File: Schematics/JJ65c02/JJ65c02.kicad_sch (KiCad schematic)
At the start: 21 parts, among them SW1 RESET, U1 74HC00

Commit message: More work on rp2040-version2
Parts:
- removed RN1: 4.7K, Resistor_THT:R_Array_SIP6, symbol Device:R_Network06_Split
- added R10, R18, R19, R8, R9: 4.7K, Resistor_THT:R_Axial_DIN0207_L6.3mm_D2.5mm_P7.62mm_Horizontal, symbol Device:R
- RAM1: footprint JJ65c02:DIP1524W45P254L4191H419Q32 -> DIP1524W45P254L4191H419Q32
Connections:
- net +5V: now also R10.1, R18.1, R19.2, R8.2, R9.2
- net GND: now also ROM1.2 (A16)
- net a15: now also ROM1.3 (A15)
- net at CPU1.2 (RDY): now also R8.1
- net at CPU1.36 (BE): now also R10.2
- net at CPU1.6 (~{NMI}): now also R9.1
- net at RAM1.30 (CE2): now also R18.2
- net at ROM1.31 (PGM): now also R19.1
- no-connect marks 24 -> 22

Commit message: Latest Kicad schematics and PCB
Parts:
- removed R10, R18, R19, R8, R9: 4.7K, Resistor_THT:R_Axial_DIN0207_L6.3mm_D2.5mm_P7.62mm_Horizontal, symbol Device:R
- added RN1, RN2: 4.7k, Resistor_THT:R_Array_SIP6, symbol Device:R_Pack03_SIP_Split
- RAM1: footprint DIP1524W45P254L4191H419Q32 -> Package_DIP:DIP-32_W15.24mm_Socket
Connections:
- net +5V: now also RN1.1 (R1.1), RN1.3 (R2.1), RN1.5 (R3.1), RN2.1 (R1.1), RN2.3 (R2.1)
- net at CPU1.2 (RDY): now also RN1.2 (R1.2)
- net at CPU1.36 (BE): now also RN1.4 (R2.2)
- net at CPU1.6 (~{NMI}): now also RN1.6 (R3.2)
- net at RAM1.30 (CE2): now also RN2.2 (R1.2)
- net at ROM1.31 (PGM): now also RN2.4 (R2.2)

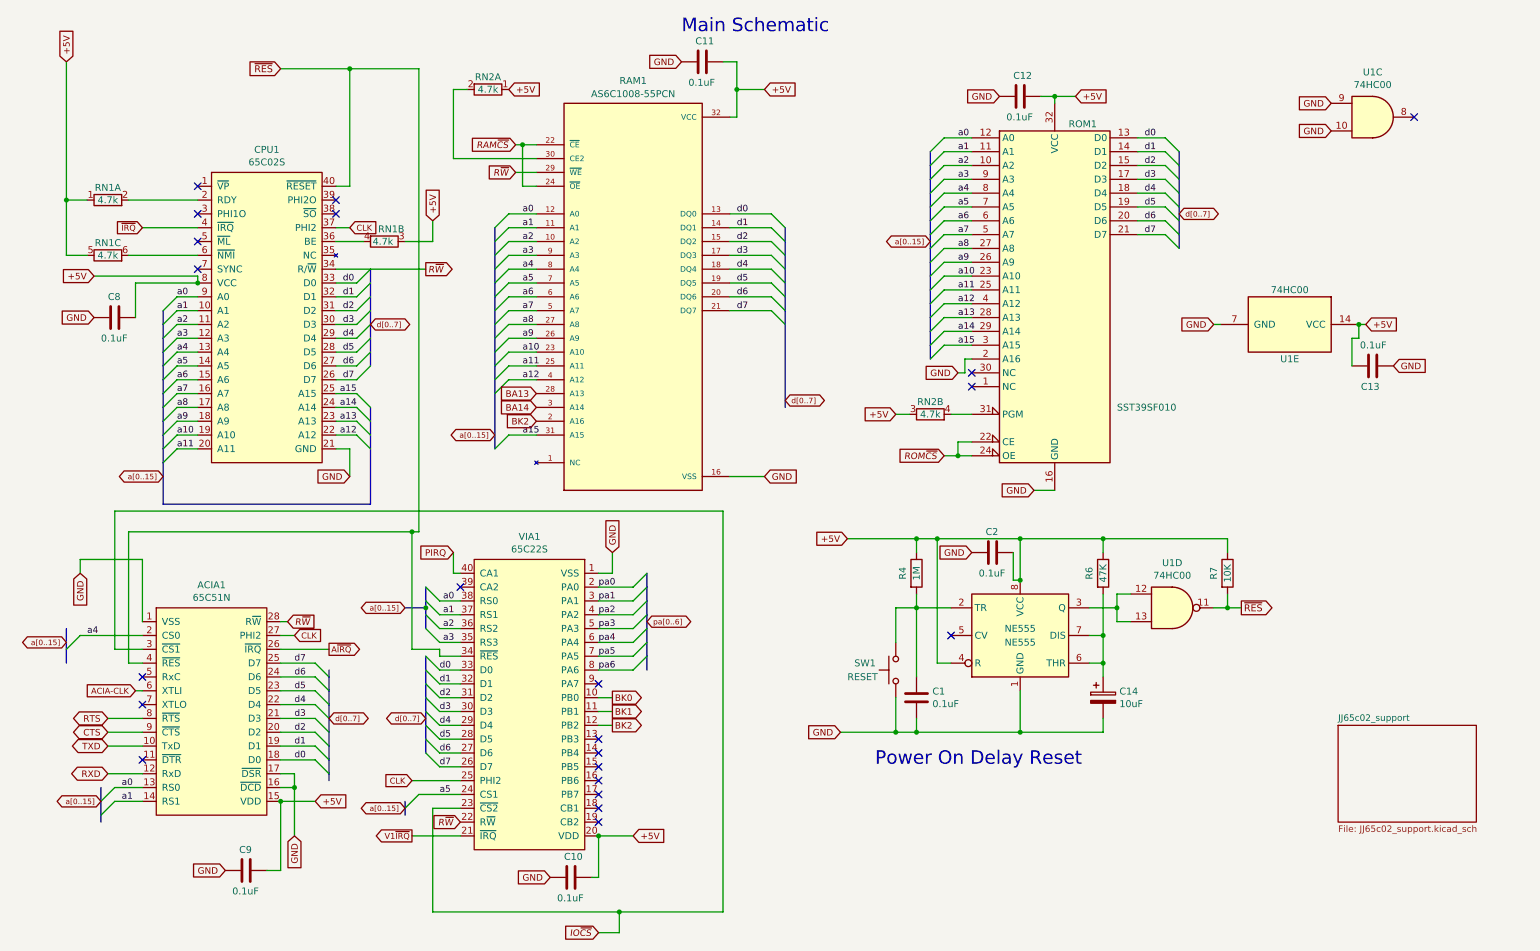
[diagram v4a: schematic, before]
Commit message: No longer use pi pico for sys clk generation - not enough pins on standard Pico board
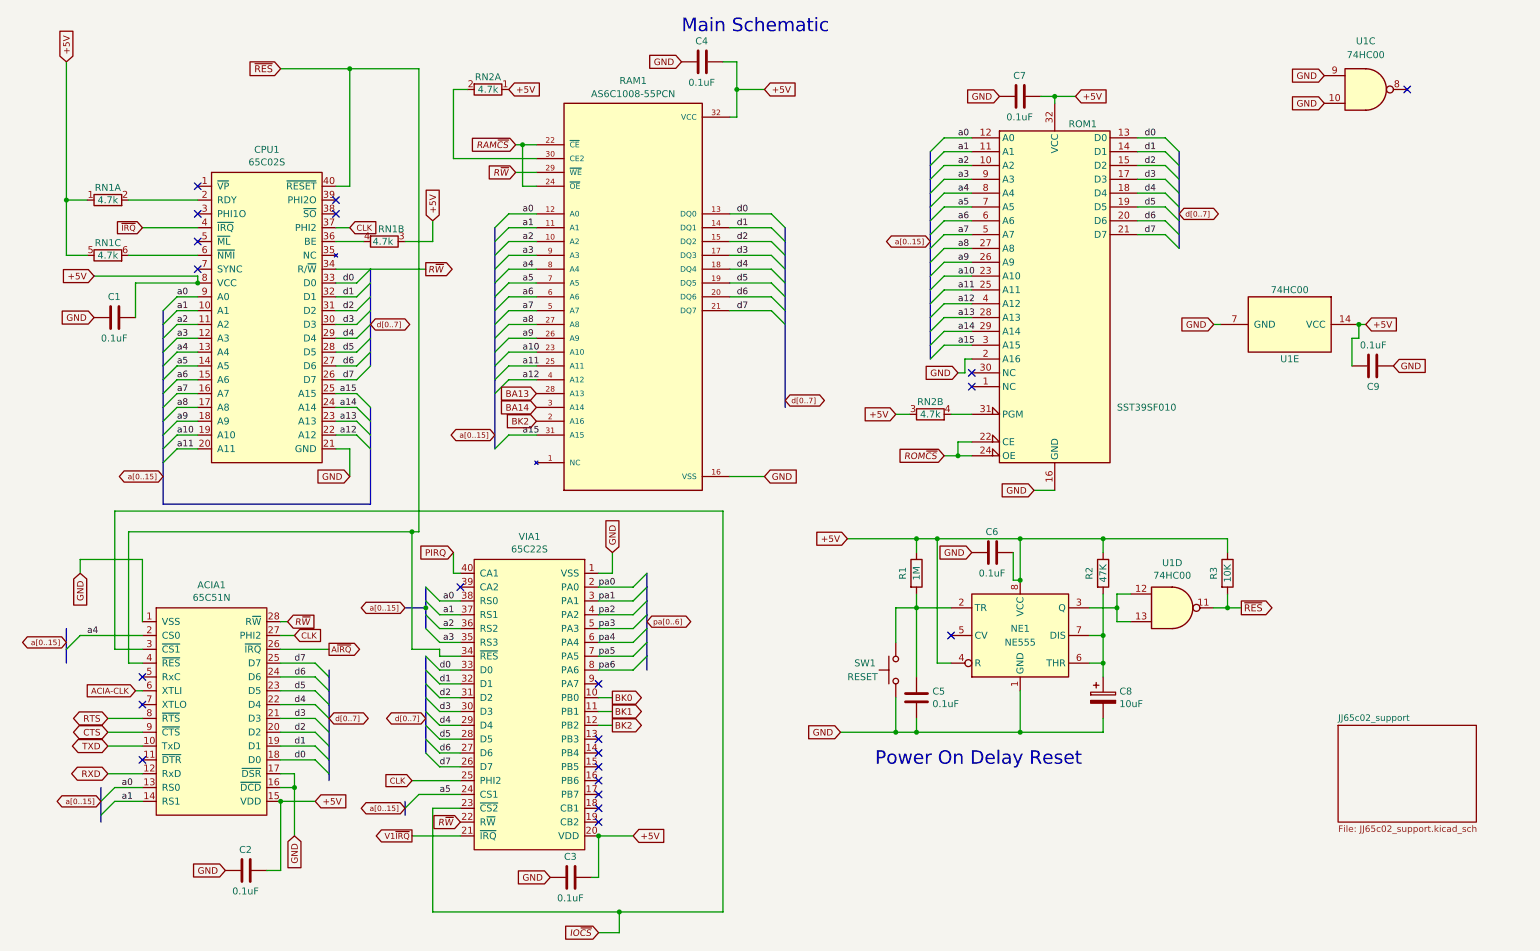
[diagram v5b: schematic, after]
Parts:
- removed unit 3 of U1
- added unit 3 of U1
- renumbered C8 to C1, C9 to C2, C10 to C3, C11 to C4, C1 to C5, C2 to C6, C12 to C7, C14 to C8, C13 to C9, NE555 to NE1, R4 to R1, R6 to R2, R7 to R3
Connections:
- net GND: now also U1.10, U1.9

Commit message: Schematic changes - Banking
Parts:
- ACIA1: symbol 6502:65C51N -> JJ65c02-rescue:65C51N-6502
- CPU1: symbol 6502:65C02S -> JJ65c02-rescue:65C02S-6502
- VIA1: symbol 6502:65C22S -> JJ65c02-rescue:65C22S-6502
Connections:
- net BK2: no longer RAM1.2 (A16)
- new net BA16: RAM1.2 (A16)
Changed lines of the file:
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@@
 	)
 	(junction
-		(at 259.08 71.12)
+		(at 62.23 158.75)
 		(diameter 0)
 		(color 0 0 0 0)
 	)
 	(junction
-		(at 212.09 110.49)
+		(at 259.08 71.12)
 		(diameter 0)
 		(color 0 0 0 0)
 	)
 	(junction
-		(at 60.96 158.75)
+		(at 212.09 110.49)
 		(diameter 0)
 		(color 0 0 0 0)
@@
 	(wire
 		(pts
-			(xy 60.96 158.75) (xy 67.31 158.75)
-		)
-		(stroke
-			(width 0)
-			(type default)
-		)
-	)
-	(wire
-		(pts
 			(xy 182.88 95.25) (xy 185.42 95.25)
 		)
@@
 	(wire
 		(pts
+			(xy 62.23 158.75) (xy 62.23 171.45)
+		)
+		(stroke
+			(width 0)
+			(type default)
+		)
+	)
+	(wire
+		(pts
 			(xy 149.86 27.94) (xy 144.78 27.94)
 		)
@@
 		)
 	)
+	(wire
+		(pts
+			(xy 64.77 156.21) (xy 63.5 156.21)
+		)
+		(stroke
+			(width 0)
+			(type default)
+		)
+	)
 	(bus
 		(pts
@@
 	(wire
 		(pts
+			(xy 62.23 158.75) (xy 67.31 158.75)
+		)
+		(stroke
+			(width 0)
+			(type default)
+		)
+	)
+	(wire
+		(pts
 			(xy 60.96 125.73) (xy 62.23 125.73)
 		)
@@
 	(wire
 		(pts
-			(xy 60.96 171.45) (xy 58.42 171.45)
+			(xy 58.42 171.45) (xy 62.23 171.45)
 		)
 		(stroke
@@
 	(wire
 		(pts
-			(xy 60.96 158.75) (xy 60.96 171.45)
-		)
-		(stroke
-			(width 0)
-			(type default)
-		)
-	)
-	(wire
-		(pts
 			(xy 102.87 55.88) (xy 107.95 55.88)
 		)
@@
 	(wire
 		(pts
+			(xy 60.96 158.75) (xy 62.23 158.75)
+		)
+		(stroke
+			(width 0)
+			(type default)
+		)
+	)
+	(wire
+		(pts
 			(xy 88.9 160.02) (xy 93.98 160.02)
 		)
@@
 	(wire
 		(pts
-			(xy 63.5 156.21) (xy 63.5 165.1)
+			(xy 64.77 156.21) (xy 64.77 165.1)
 		)
 		(stroke
@@
 		)
 		(property "Intersheetrefs" "${INTERSHEET_REFS}"
-			(at 44.9772 171.3754 0)
+			(at 44.9709 171.45 0)
 			(effects
 				(font
@@
 	(global_label "+5V"
 		(shape input)
+		(at 67.31 158.75 0)
+		(fields_autoplaced yes)
+		(effects
+			(font
+				(size 1.1938 1.1938)
+			)
+			(justify left)
+		)
+		(property "Intersheetrefs" "${INTERSHEET_REFS}"
+			(at 73.1392 158.75 0)
+			(effects
+				(font
+					(size 1.27 1.27)
+				)
+				(justify left)
+				(hide yes)
+			)
+		)
+	)
+	(global_label "+5V"
+		(shape input)
 		(at 165.1 110.49 180)
 		(fields_autoplaced yes)
@@
 		)
 	)
-	(global_label "+5V"
-		(shape input)
-		(at 67.31 158.75 0)
-		(fields_autoplaced yes)
-		(effects
-			(font
-				(size 1.1938 1.1938)
-			)
-			(justify left)
-		)
-		(property "Intersheetrefs" "${INTERSHEET_REFS}"
-			(at 73.1392 158.75 0)
-			(effects
-				(font
-					(size 1.27 1.27)
-				)
-				(justify left)
-				(hide yes)
-			)
-		)
-	)
 	(global_label "R~{W}"
 		(shape output)
@@
 		)
 		(property "Intersheetrefs" "${INTERSHEET_REFS}"
-			(at 104.6672 172.6454 0)
+			(at 104.6609 172.72 0)
 			(effects
 				(font
@@
 	(global_label "GND"
 		(shape input)
-		(at 63.5 165.1 270)
+		(at 64.77 165.1 270)
+		(fields_autoplaced yes)
+		(effects
+			(font
+				(size 1.1938 1.1938)
+			)
+			(justify right)
+		)
+		(property "Intersheetrefs" "${INTERSHEET_REFS}"
+			(at 64.77 170.9291 90)
+			(effects
+				(font
+					(size 1.27 1.27)
+				)
+				(justify right)
+				(hide yes)
+			)
+		)
+	)
+	(global_label "BA16"
+		(shape input)
+		(at 107.95 88.9 180)
 		(fields_autoplaced yes)
 		(effects
@@
 		)
 		(property "Intersheetrefs" "${INTERSHEET_REFS}"
-			(at 63.5 170.9291 90)
+			(at 101.268 88.9 0)
 			(effects
 				(font
@@
 		)
 	)
-	(global_label "BK2"
-		(shape input)
-		(at 107.95 88.9 180)
-		(fields_autoplaced yes)
-		(effects
-			(font
-				(size 1.1938 1.1938)
-			)
-			(justify right)
-		)
-		(property "Intersheetrefs" "${INTERSHEET_REFS}"
-			(at 102.2345 88.9 0)
-			(effects
-				(font
-					(size 1.27 1.27)
-				)
-				(justify right)
-				(hide yes)
-			)
-		)
-	)
 	(global_label "+5V"
 		(shape input)
@@
 	)
 	(symbol
-		(lib_id "6502:65C02S")
+		(lib_id "JJ65c02-rescue:65C02S-6502")
 		(at 58.42 68.58 0)
 		(unit 1)
@@
 	)
 	(symbol
-		(lib_id "6502:65C22S")
+		(lib_id "JJ65c02-rescue:65C22S-6502")
 		(at 106.68 139.7 0)
 		(mirror y)
@@
 	)
 	(symbol
-		(lib_id "6502:65C51N")
+		(lib_id "JJ65c02-rescue:65C51N-6502")
 		(at 48.26 142.24 0)
 		(unit 1)
